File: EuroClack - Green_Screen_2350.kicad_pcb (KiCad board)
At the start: 4 copper layers, 109.2 x 110 mm, 272 parts, among them J1 C2982548, J10 CV_OUT_4, J11 C7471773, J12 Pin Header, J13 CV_GATE_IN_4, J14 AUDIO_OUT_1, J15 AUDIO_IN_1, J16 C168704, J17 USB_HOST, J18 Eurorack 10 pin socket, J19 C7470101, J2 AUDIO_IN_2, J20 STEMMA_QT, J21 C2856837, J22 C2856837, J23 CV_GATE_IN3, J24 CV_GATE_IN_4, J25 SM03B-SRSS-TB, J26 CV_OUT_3, J27 CV_OUT_4, J28 C2881890, J29 C7470089, J3 CV_GATE_IN_1, J30 FFC, J31 SM03B-SRSS-TB, J4 CV_GATE_IN_2, J5 CV_GATE_IN3, J6 AUDIO_OUT_2, J7 CV_OUT_1, J8 CV_OUT_2, J9 CV_OUT_3, Q1 A3400A, Q2 A3401A, Q3 A3401A, Q4 A3400A, SW3 RotaryEncoder_Switch, SW4 RotaryEncoder_Switch, SW5 USER2, SW6 SW_Push, SW7 SW_Push, U1 RP2350_80QFN, U10 SPX3819M5-L-5-0, U11 TL072, U12 TPS54302, U13 TL072, U14 SPX3819M5-L-3-3, U15 SRAM, U16 SPX3819M5-L-3-3, U17 TL072, U18 SN74LVC1T45DCK, U19 LM393, U2 PCM5102, U20 TL072, U21 LM393, U22 SN74LVC1T45DCK, U23 TPS54302, U3 MCP4728, U4 W25Q128JVS, U5 PCM1808PWR, U6 TL072, U7 REF3033, U8 TL072, U9 SPX3819M5-L-3-3, Y1 ABM8-272-T3

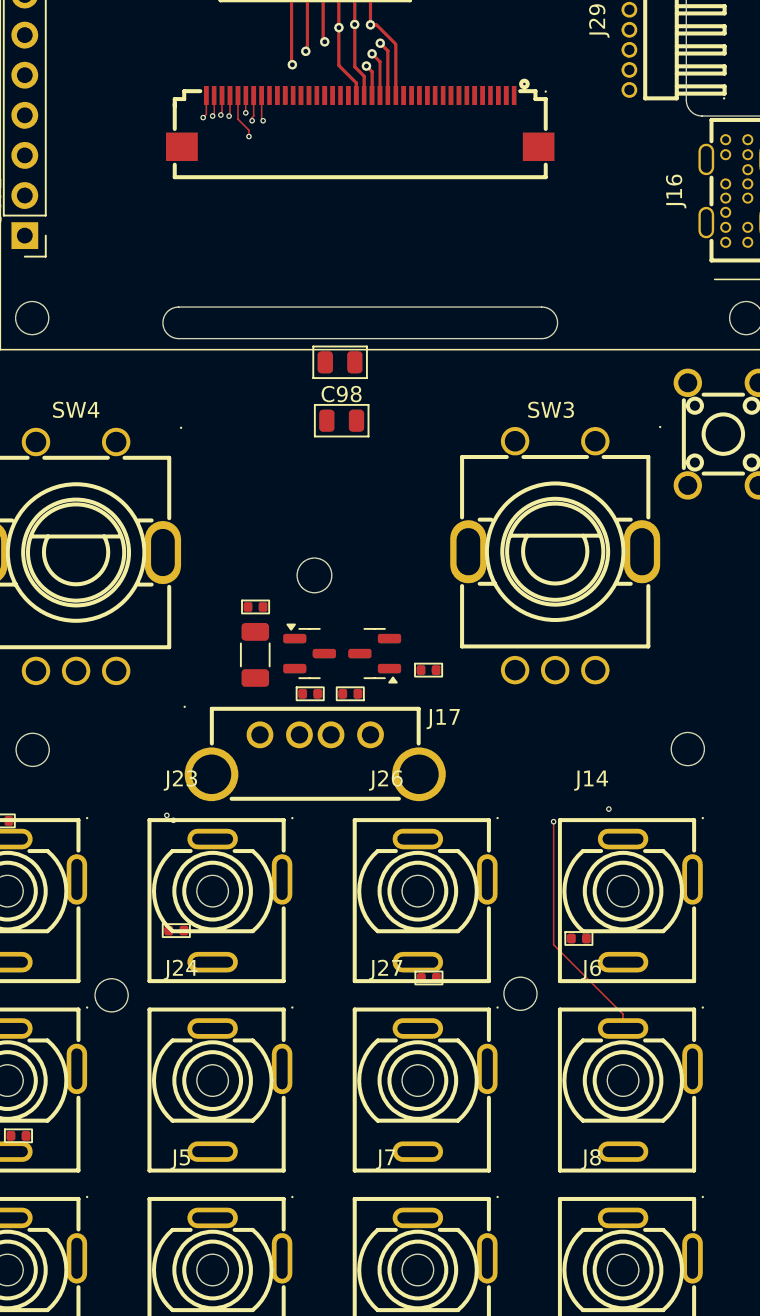
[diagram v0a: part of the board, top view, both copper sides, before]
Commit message: Panel routing
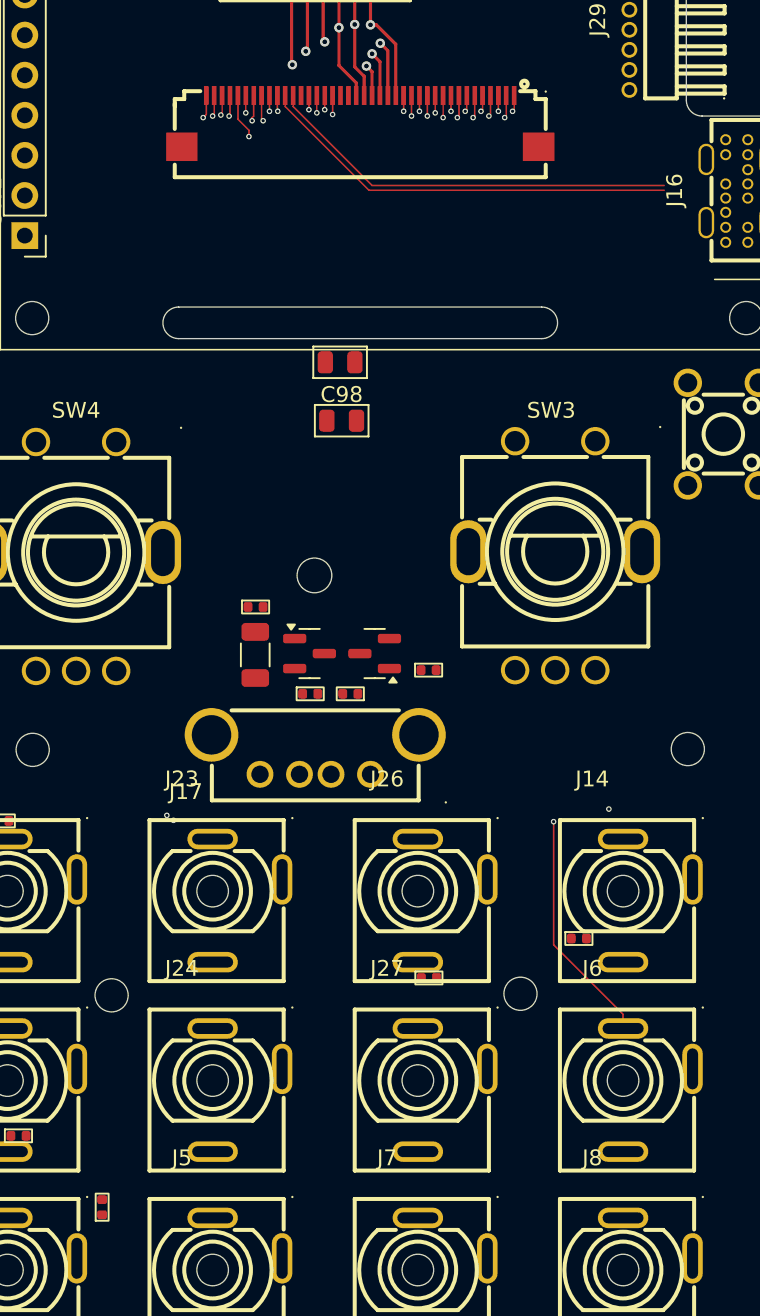
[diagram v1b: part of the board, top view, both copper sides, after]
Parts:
- moved R87 18.1 mm to (92.8, 140.0), turned to 90 degrees
- turned J17 to 180 degrees
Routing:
- net /USB_HOST_DP_JACK: track 0.00 -> 52.4 mm, vias 0 -> 1
- net /USB_HOST_DM_JACK: track 0.00 -> 52.1 mm, vias 0 -> 1
- net /USB_DP_JACK: track 0.00 -> 26.9 mm
- net /USB_DM_JACK: track 0.00 -> 26.3 mm
- net /ENC2_SW_JACK: track 0.00 -> 1.44 mm, vias 0 -> 1
- net /ENC2_B_JACK: track 0.00 -> 1.44 mm, vias 0 -> 1
- net /CV_OUT_3_JACK: track 0.00 -> 1.44 mm, vias 0 -> 1
- net /ENC1_A_JACK: track 0.00 -> 1.40 mm, vias 0 -> 1
- net /CV_OUT_2_JACK: track 0.00 -> 1.34 mm, vias 0 -> 1
- net /SW_USR2_JACK: track 0.00 -> 1.30 mm, vias 0 -> 1
- net /SW_RUN_JACK: track 0.00 -> 1.30 mm, vias 0 -> 1
- net /5V_JACK: track 0.00 -> 1.20 mm, vias 0 -> 1
- net /ENC1_SW_JACK: track 0.00 -> 1.10 mm, vias 0 -> 1
- net /CV_IN_1_JACK: track 0.00 -> 1.10 mm, vias 0 -> 1
- net /~{USBH_PWR_EN_JACK}: track 0.00 -> 1.04 mm, vias 0 -> 1
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
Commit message: Physical prototypes tested, needed shifting
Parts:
- removed C88: 10u, Clacktronics:C_0805_2012Metric
- removed the REF** at (88.4, 55.5)
- removed the REF** at (129.9, 55.5)
- moved R93 60.1 mm to (122.9, 68.5), turned to 90 degrees
- moved R94 60.0 mm to (124.0, 68.8), turned to -90 degrees
- moved R86 49.8 mm to (81.5, 116.8)
- moved R98 49.6 mm to (119.7, 61.0), turned to 180 degrees
- moved R97 49.0 mm to (119.7, 59.9)
- moved U23 48.7 mm to (116.6, 61.5), turned to 90 degrees
- moved C86 45.5 mm to (114.2, 60.4), turned to -90 degrees
- moved C87 44.4 mm to (123.0, 55.6)
- moved L4 42.4 mm to (116.6, 55.9), turned to -90 degrees
- moved C89 41.4 mm to (123.5, 59.2)
- moved C85 39.2 mm to (118.3, 64.3), turned to 180 degrees
- moved R88 35.6 mm to (88.5, 150.8), turned to 180 degrees
- moved C36 32.0 mm to (103.0, 54.9), turned to 180 degrees
- moved C98 29.4 mm to (123.9, 65.5), turned to -90 degrees
- moved REF** 5.01 mm to (129.1, 81.5)
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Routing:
- net /CV_IN_2_JACK: track 0.90 -> 127.4 mm, vias 1 -> 3
- net /CV_OUT_4_JACK: track 1.00 -> 89.8 mm, vias 1 -> 2
- net /CV_OUT_3_JACK: track 1.44 -> 88.1 mm, vias 1 -> 2
- net /CV_IN_1_JACK: track 1.10 -> 84.2 mm, vias 1 -> 2
- net /CV_OUT_2_JACK: track 1.34 -> 81.1 mm, vias 1 -> 2
- net /GATE_OUT_2_JACK: track 0.90 -> 75.9 mm
- net /CV_OUT_1_JACK: track 1.04 -> 75.9 mm, vias 1 -> 2
- net /3V3_SD_SCREEN: track 0.00 -> 61.5 mm
- net /GATE_OUT_1_JACK: track 0.00 -> 61.2 mm, vias 0 -> 1
- net /ENC2_A_JACK: track 1.04 -> 44.1 mm, vias 1 -> 2
- net /ENC2_B_JACK: track 1.44 -> 44.5 mm, vias 1 -> 2
- net /5V_JACK: track 1.20 -> 43.9 mm
- net /SW_USR2_JACK: track 1.30 -> 42.3 mm
- net /ENC1_B_JACK: track 1.00 -> 41.6 mm
- net /ENC1_A_JACK: track 1.40 -> 41.9 mm
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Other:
- outline, holes or cut-outs redrawn

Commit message: More changes
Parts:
- removed SW5: USER2, green_screen:SW-TH_4P-L5.0-W5.0-P4.50-LS6.5
- added SW2: ~, EasyEDA_Lib:SW-TH_PS-8556DVA-6PN, F.Cu at (82.2, 78.1)
- J17: footprint green_screen:USB-A-SMD_AF180-13.1 -> green_screen:USB-A-TH_C42536
- SW1: footprint green_screen:SW-TH_4P-L5.0-W5.0-P4.50-LS6.5 -> EasyEDA_Lib:SW-TH_PS-8556DVA-6PN
- moved R95 79.5 mm to (106.5, 116.6), turned to 90 degrees
- moved R96 70.5 mm to (106.6, 128.4), turned to 90 degrees
- moved J16 53.1 mm to (82.3, 91.5)
- moved SW6 50.5 mm to (132.1, 96.1), turned to -90 degrees
- moved SW1 16.6 mm to (82.2, 59.7), turned to 0 degrees
- moved J12 4.00 mm to (90.1, 77.4)
- moved J19 4.00 mm to (35.9, 64.8)
- moved REF** 4.00 mm to (90.1, 111.0)
- moved REF** 4.00 mm to (133.1, 111.0)
- moved REF** 4.00 mm to (133.1, 81.5)
- moved REF** 4.00 mm to (90.1, 81.5)
- moved REF** 4.00 mm to (133.1, 55.5)
- moved REF** 4.00 mm to (90.1, 55.5)
- moved SW7 3.60 mm to (132.1, 87.4), turned to 90 degrees
- moved J22 1.96 mm to (111.1, 71.0)
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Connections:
- SW1 pad 1: /SW_USR1_JACK -> GND_JACK
- SW1 pad 2: GND_JACK -> /SW_USR1_JACK
- SW1 pad 3: (no net) -> unconnected-(SW1-Pad3)
- SW1 pad 4: (no net) -> unconnected-(SW1-Pad4)
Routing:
- net /CV_IN_1_JACK: track 84.2 -> 0.00 mm, vias 2 -> 0
- net /USB_DP_JACK: track 27.1 -> 84.2 mm, vias 0 -> 2
- net /ENC2_A_JACK: track 44.1 -> 0.00 mm, vias 2 -> 0
- net /GATE_OUT_1_JACK: track 61.2 -> 105.1 mm, vias 1 -> 2
- net /5V_JACK: track 43.9 -> 0.00 mm, vias 1 -> 0
- net /ENC1_SW_JACK: track 1.10 -> 44.1 mm, vias 1 -> 2
- net /12V_JACK: track 13.5 -> 55.8 mm, vias 0 -> 1
- net /SW_USR2_JACK: track 42.3 -> 1.10 mm
- net /DISPLAY_RES_JACK: track 36.4 -> 64.1 mm, vias 2 -> 4
- net /GATE_IN_1_JACK: track 54.5 -> 81.6 mm
- net /USB_DM_JACK: track 26.6 -> 0.00 mm
- net /GATE_IN_2_JACK: track 69.0 -> 95.6 mm
- net /SW_RUN_JACK: track 25.1 -> 0.00 mm, vias 2 -> 0
- net /DISPLAY_SDA_JACK: track 36.9 -> 54.4 mm, vias 2 -> 4
- net /~{SW_MENU_BOOT_JACK}: track 17.5 -> 1.10 mm, vias 2 -> 1
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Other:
- outline, holes or cut-outs redrawn
